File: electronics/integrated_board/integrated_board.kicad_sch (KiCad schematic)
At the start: 67 parts, among them CON1 BARREL_JACK, J1 rot_encoderZ(35,34), J10 pcf8575 IO expander, J11 Switch 1, J13 motor1(15,2,0,4), J15 motor2 (16,17,5,18), J17 motor3 (19,21,22,23), J2 rot_encoderY(25,26), J3 rot_encoderX(14,27), J4 Switch 2, J5 Endstop A, J6 Endstop B, J7 Endstop C, J8 Conn_01x16, J9 Conn_01x16, P1 Conn_01x02, P10 Conn_01x02, P15 Conn_01x02, P16 UART, P2 LCD, U1 ULN2003, U2 ULN2003, U3 LM2596T-5, U4 ESP32-DEVKITC-32D

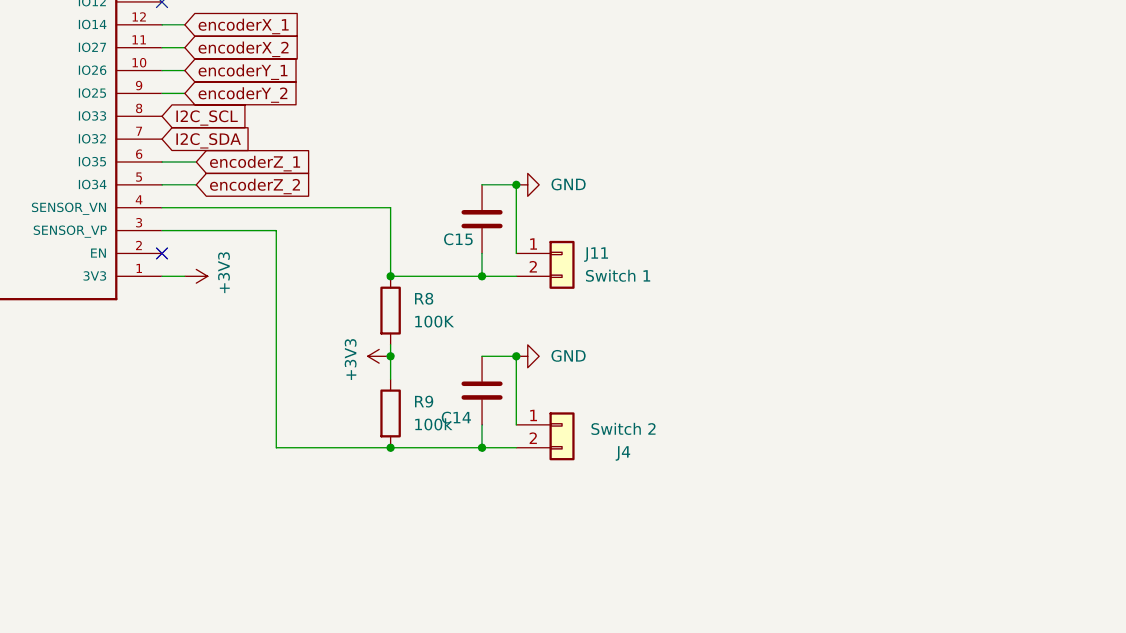
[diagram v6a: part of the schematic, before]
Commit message: Updated PCB
reintroduced voltage divider for switch 1 and 2 as pull up
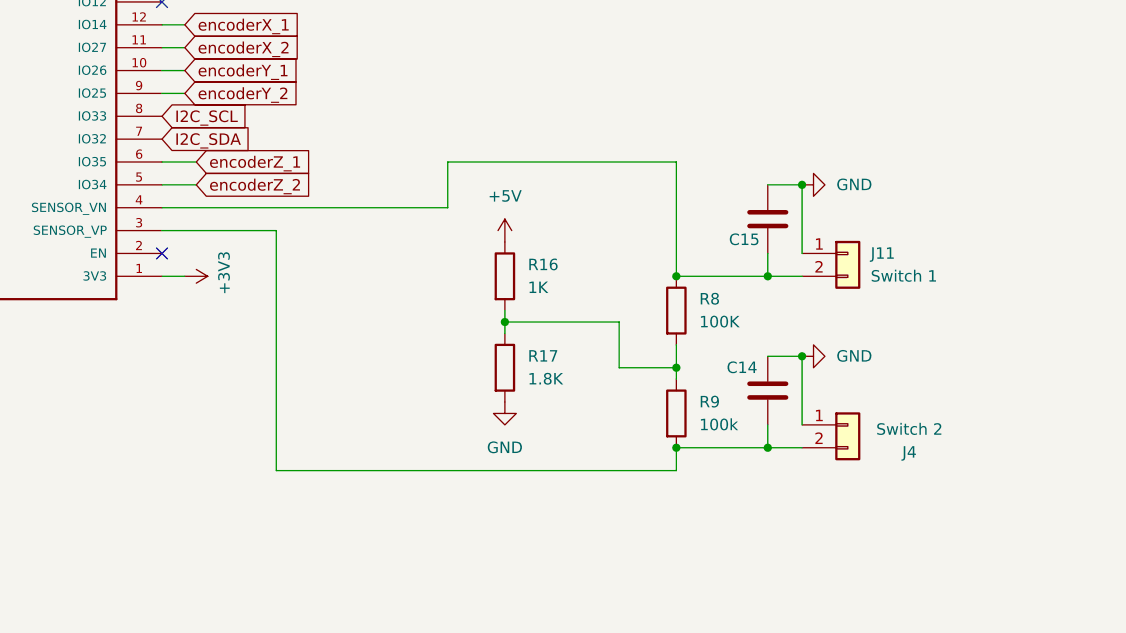
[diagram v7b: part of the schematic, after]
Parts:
- added R16: 1K, Resistor_THT:R_Axial_DIN0309_L9.0mm_D3.2mm_P12.70mm_Horizontal, symbol Device:R
- added R17: 1.8K, Resistor_THT:R_Axial_DIN0309_L9.0mm_D3.2mm_P12.70mm_Horizontal, symbol Device:R
- C14, C15: value C -> 33nF
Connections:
- net +3V3: no longer R8.2, R9.1
- net +5V: now also R16.1
- net GND: now also R17.2
- new net: R16.2, R17.1, R8.2, R9.1
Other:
- moved on the sheet: C14, C15, J11, J4, R8, R9

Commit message: Updated endstop protocol
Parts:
- C12, C13, C7: value C -> 33nF
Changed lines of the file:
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@@
 			)
 		)
-		(property "Value" "C"
+		(property "Value" "33nF"
 			(at 146.05 243.8401 0)
 			(effects
@@
 			)
 		)
-		(property "Value" "C"
+		(property "Value" "33nF"
 			(at 146.05 227.3301 0)
 			(effects
@@
 			)
 		)
-		(property "Value" "C"
+		(property "Value" "33nF"
 			(at 146.05 260.3501 0)
 			(effects
